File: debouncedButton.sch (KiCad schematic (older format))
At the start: 4 parts, among them SW1 SW_Push

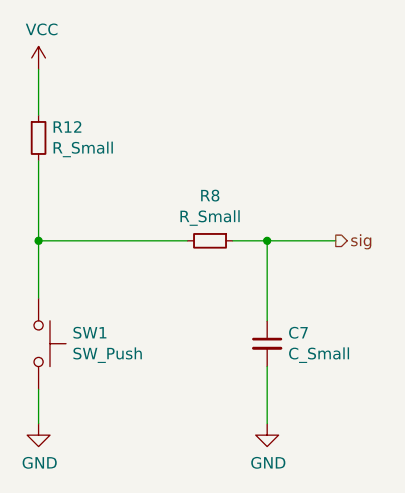
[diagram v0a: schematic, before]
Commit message: rev 1a, XO fixed, more labels and rearranging
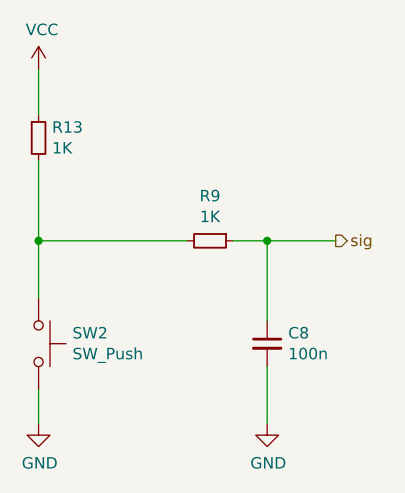
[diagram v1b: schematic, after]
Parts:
- C7: value C_Small -> 100n
- R12, R8: value R_Small -> 1K
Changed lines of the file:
@@
 AR Path="/604568F4/60456C1B/60467F6B" Ref="C7"  Part="1"
 AR Path="/604568F4/60456C34/60467F6B" Ref="C8"  Part="1"
-F 0 "C7" H 5292 2346 50  0000 L CNN
-F 1 "C_Small" H 5292 2255 50  0000 L CNN
+F 0 "C8" H 5292 2346 50  0000 L CNN
+F 1 "100n" H 5292 2255 50  0000 L CNN
 F 2 "Capacitor_SMD:C_0603_1608Metric" H 5200 2300 50  0001 C CNN
 F 3 "~" H 5200 2300 50  0001 C CNN
@@
 AR Path="/604568F4/60456C1B/60469373" Ref="R8"  Part="1"
 AR Path="/604568F4/60456C34/60469373" Ref="R9"  Part="1"
-F 0 "R8" V 4754 1850 50  0000 C CNN
-F 1 "R_Small" V 4845 1850 50  0000 C CNN
+F 0 "R9" V 4754 1850 50  0000 C CNN
+F 1 "1K" V 4845 1850 50  0000 C CNN
 F 2 "Resistor_SMD:R_0603_1608Metric" H 4950 1850 50  0001 C CNN
 F 3 "~" H 4950 1850 50  0001 C CNN
@@
 AR Path="/604568F4/60456C1B/60469AB8" Ref="#PWR0119"  Part="1"
 AR Path="/604568F4/60456C34/60469AB8" Ref="#PWR0121"  Part="1"
-F 0 "#PWR0119" H 4200 2400 50  0001 C CNN
+F 0 "#PWR0121" H 4200 2400 50  0001 C CNN
 F 1 "GND" H 4205 2477 50  0000 C CNN
 F 2 "" H 4200 2650 50  0001 C CNN
@@
 AR Path="/604568F4/60456C1B/60469E85" Ref="#PWR0120"  Part="1"
 AR Path="/604568F4/60456C34/60469E85" Ref="#PWR0122"  Part="1"
-F 0 "#PWR0120" H 5200 2400 50  0001 C CNN
+F 0 "#PWR0122" H 5200 2400 50  0001 C CNN
 F 1 "GND" H 5205 2477 50  0000 C CNN
 F 2 "" H 5200 2650 50  0001 C CNN
@@
 AR Path="/604568F4/60456C1B/604A22C9" Ref="SW1"  Part="1"
 AR Path="/604568F4/60456C34/604A22C9" Ref="SW2"  Part="1"
-F 0 "SW1" V 4154 2448 50  0000 L CNN
+F 0 "SW2" V 4154 2448 50  0000 L CNN
 F 1 "SW_Push" V 4245 2448 50  0000 L CNN
 F 2 "Button_Switch_THT:SW_PUSH_6mm" H 4200 2500 50  0001 C CNN
@@
 AR Path="/604568F4/60456C1B/604AFB0E" Ref="R12"  Part="1"
 AR Path="/604568F4/60456C34/604AFB0E" Ref="R13"  Part="1"
-F 0 "R12" H 4259 1446 50  0000 L CNN
-F 1 "R_Small" H 4259 1355 50  0000 L CNN
+F 0 "R13" H 4259 1446 50  0000 L CNN
+F 1 "1K" H 4259 1355 50  0000 L CNN
 F 2 "Resistor_SMD:R_0603_1608Metric" H 4200 1400 50  0001 C CNN
 F 3 "~" H 4200 1400 50  0001 C CNN
@@
 AR Path="/604568F4/60456C1B/604B16FA" Ref="#PWR0125"  Part="1"
 AR Path="/604568F4/60456C34/604B16FA" Ref="#PWR0126"  Part="1"
-F 0 "#PWR0125" H 4200 950 50  0001 C CNN
+F 0 "#PWR0126" H 4200 950 50  0001 C CNN
 F 1 "VCC" H 4215 1273 50  0000 C CNN
 F 2 "" H 4200 1100 50  0001 C CNN
